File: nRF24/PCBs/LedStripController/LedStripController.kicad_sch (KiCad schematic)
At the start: 11 parts, among them J1 Conn_01x04, M1 TP4056, U1 NRF24L01, U2 ATtiny84, U3 MCP1700x-330

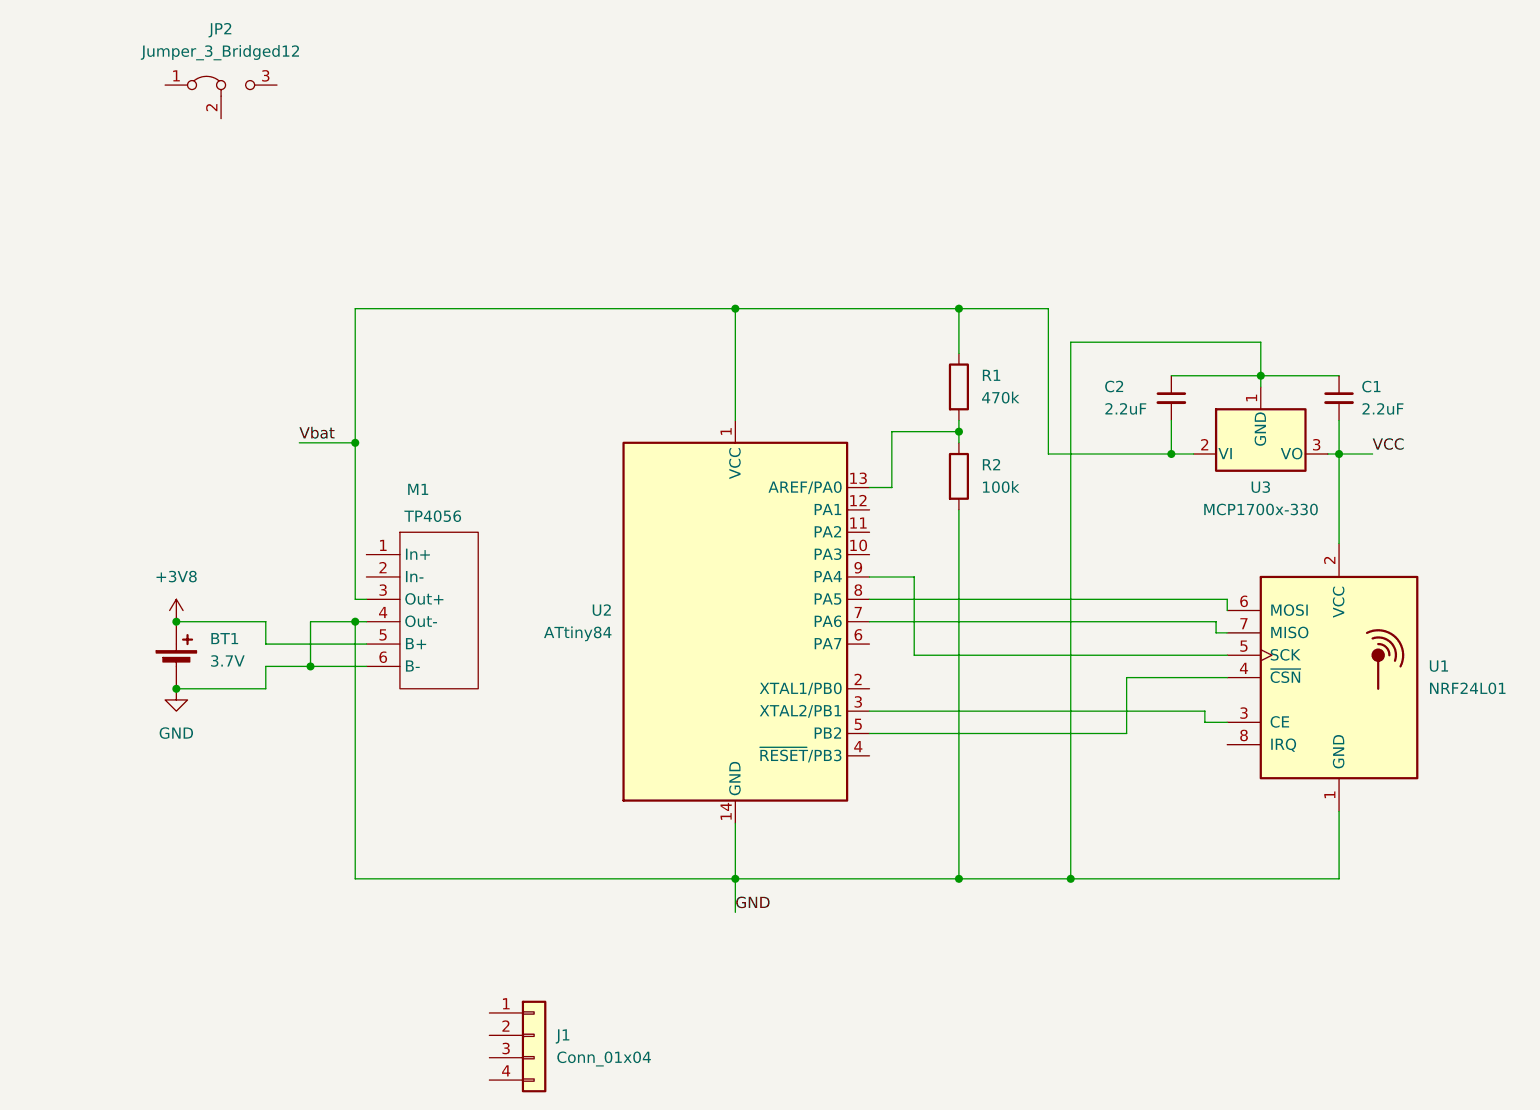
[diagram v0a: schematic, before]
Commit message: LED Strip Controller and Programming Adapter WIP
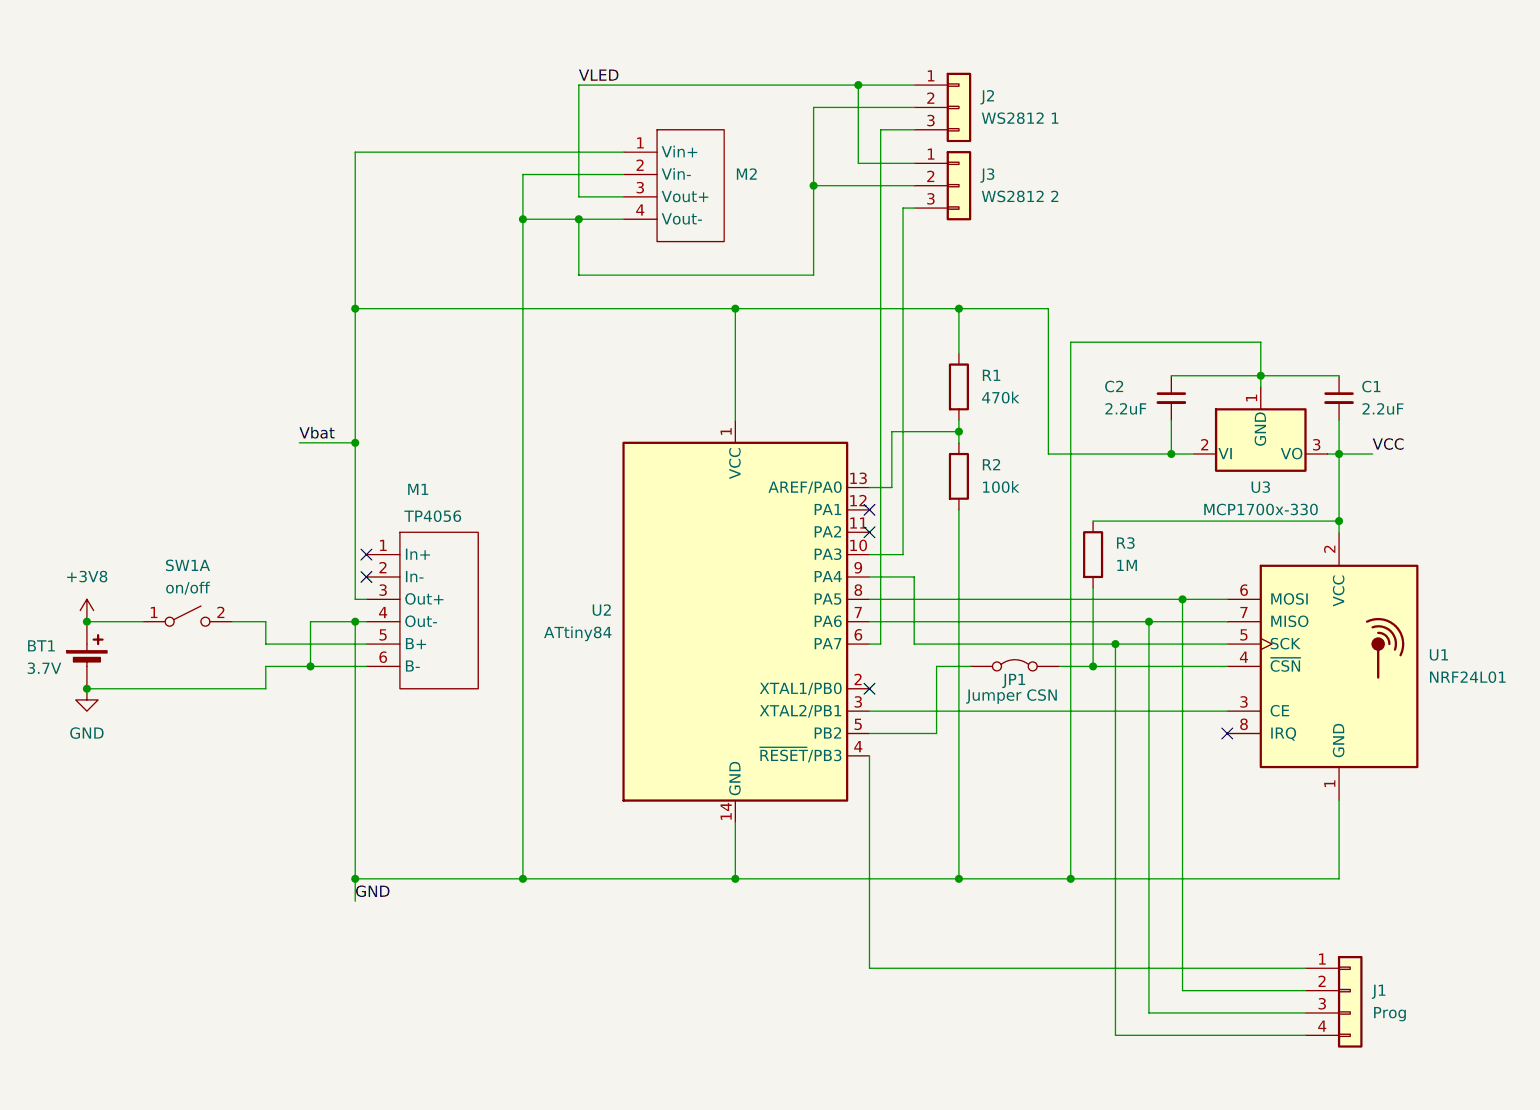
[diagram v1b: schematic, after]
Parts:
- removed JP2: Jumper_3_Bridged12, symbol Jumper:Jumper_3_Bridged12
- added J2: WS2812 1, hagego:JST_XH_1x03_P2.54, symbol Connector_Generic:Conn_01x03
- added J3: WS2812 2, hagego:JST_XH_1x03_P2.54, symbol Connector_Generic:Conn_01x03
- added JP1: Jumper CSN, Connector_PinHeader_2.54mm:PinHeader_2x01_P2.54mm_Vertical, symbol Jumper:Jumper_2_Bridged
- added M2: ~, hagego:MT3608_Module, symbol hagego:MT3608_Module
- added R3: 1M, Resistor_THT:R_Axial_DIN0207_L6.3mm_D2.5mm_P10.16mm_Horizontal, symbol Device:R
- added SW1: on/off, hagego:SwitchHorizontal_SK-12F14, symbol Switch:SW_DPST_x2
- J1: value Conn_01x04 -> Prog
- U2: footprint Package_DIP:DIP-14_W7.62mm_Socket -> Package_DIP:DIP-14_W7.62mm
- U3: footprint Package_TO_SOT_THT:TO-92_HandSolder -> Package_TO_SOT_THT:TO-92_Inline
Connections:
- net +3V8: now also SW1.1 (A); no longer M1.5 (B+)
- net GND: now also J2.2 (Pin_2), J3.2 (Pin_2), M2.2 (Vin-), M2.4 (Vout-)
- net VCC: now also R3.1
- net Vbat: now also M2.1 (Vin+)
- net at U1.4 (~{CSN}): now also JP1.2 (B), R3.2; no longer U2.5 (PB2)
- net at U1.5 (SCK), U2.9 (PA4): now also J1.4 (Pin_4)
- net at U1.6 (MOSI), U2.8 (PA5): now also J1.2 (Pin_2)
- net at U1.7 (MISO), U2.7 (PA6): now also J1.3 (Pin_3)
- net at U2.10 (PA3): now also J3.3 (Pin_3)
- net at U2.4 (~{RESET}/PB3): now also J1.1 (Pin_1)
- net at U2.6 (PA7): now also J2.3 (Pin_3)
- new net: M1.5 (B+), SW1.2 (B)
- new net: JP1.1 (A), U2.5 (PB2)
- new net VLED: J2.1 (Pin_1), J3.1 (Pin_1), M2.3 (Vout+)
- no-connect marks 0 -> 6
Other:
- moved on the sheet: BT1, J1, U1

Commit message: LED Strip Controller production version
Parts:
- added D1: LED, LED_THT:LED_D3.0mm, symbol Device:LED
- added J4: Bat 2, hagego:JST_XH_1x02_P2.54, symbol Connector:Conn_01x02_Socket
- added R4: 100, Resistor_THT:R_Axial_DIN0207_L6.3mm_D2.5mm_P10.16mm_Horizontal, symbol Device:R
- Bat1: renamed from BT1; footprint hagego:JST_XH_1x02_P2.54 -> hagego:JST_PH_1x02_P2.00
- J1: footprint hagego:JST_XH_1x04_P2.54 -> Connector_PinHeader_2.54mm:PinHeader_1x04_P2.54mm_Vertical
- U3: footprint Package_TO_SOT_THT:TO-92_Inline -> Package_TO_SOT_THT:TO-92_HandSolder
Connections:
- net +3V8: now also J4.1 (Pin_1)
- net GND: now also D1.1 (K), J4.2 (Pin_2)
- net at M1.5 (B+), SW1.2 (B): now also R4.1
- net MOSI: now reaches J1.2 (Pin_2), U1.6 (MOSI), U2.8 (PA5)
- net MISO: now reaches J1.3 (Pin_3), U1.7 (MISO), U2.7 (PA6)
- new net: D1.2 (A), R4.2

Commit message: nRF24 LED Strip Controller Debugging
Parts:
- removed JP1: Jumper CSN, Connector_PinHeader_2.54mm:PinHeader_2x01_P2.54mm_Vertical, symbol Jumper:Jumper_2_Bridged
- M2: value ~ -> (none)
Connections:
- net at R3.2, U1.4 (~{CSN}): now also U2.5 (PB2)
- net at U1.5 (SCK), U2.9 (PA4): now also J1.1 (Pin_1); no longer J1.4 (Pin_4)
- net at U2.4 (~{RESET}/PB3): now also J1.4 (Pin_4); no longer J1.1 (Pin_1)
